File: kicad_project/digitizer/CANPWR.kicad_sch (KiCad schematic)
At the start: 4 parts

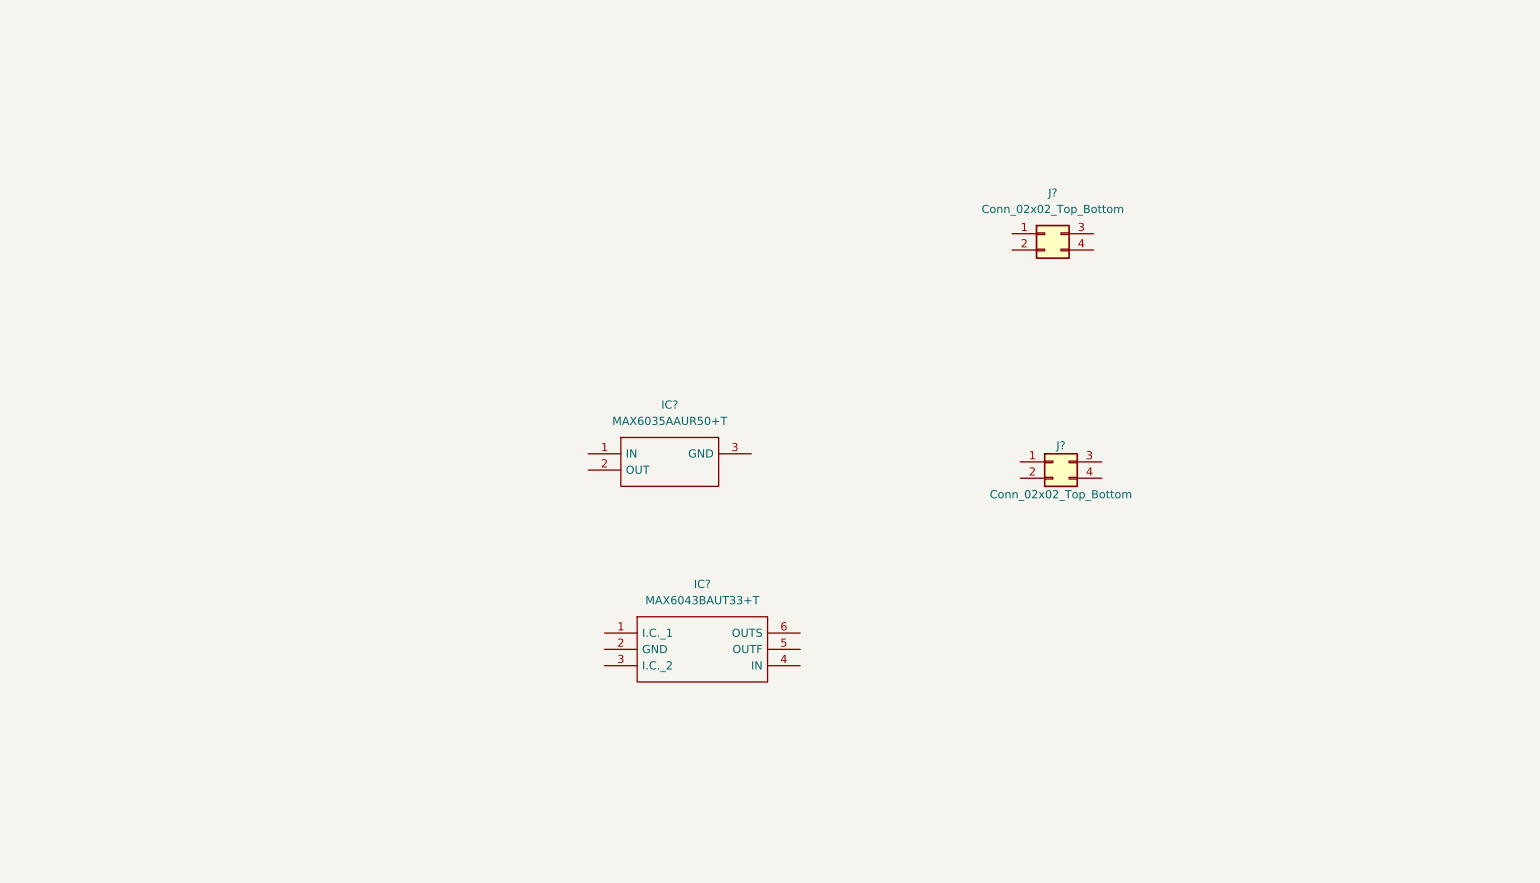
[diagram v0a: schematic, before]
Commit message: finished the CANPWR sheet, got to work on the MCU sheet (finished the CAN stuff). Good progress; still missing the MCU pin connections and the connector footprints (M12, deutsch, etc.)
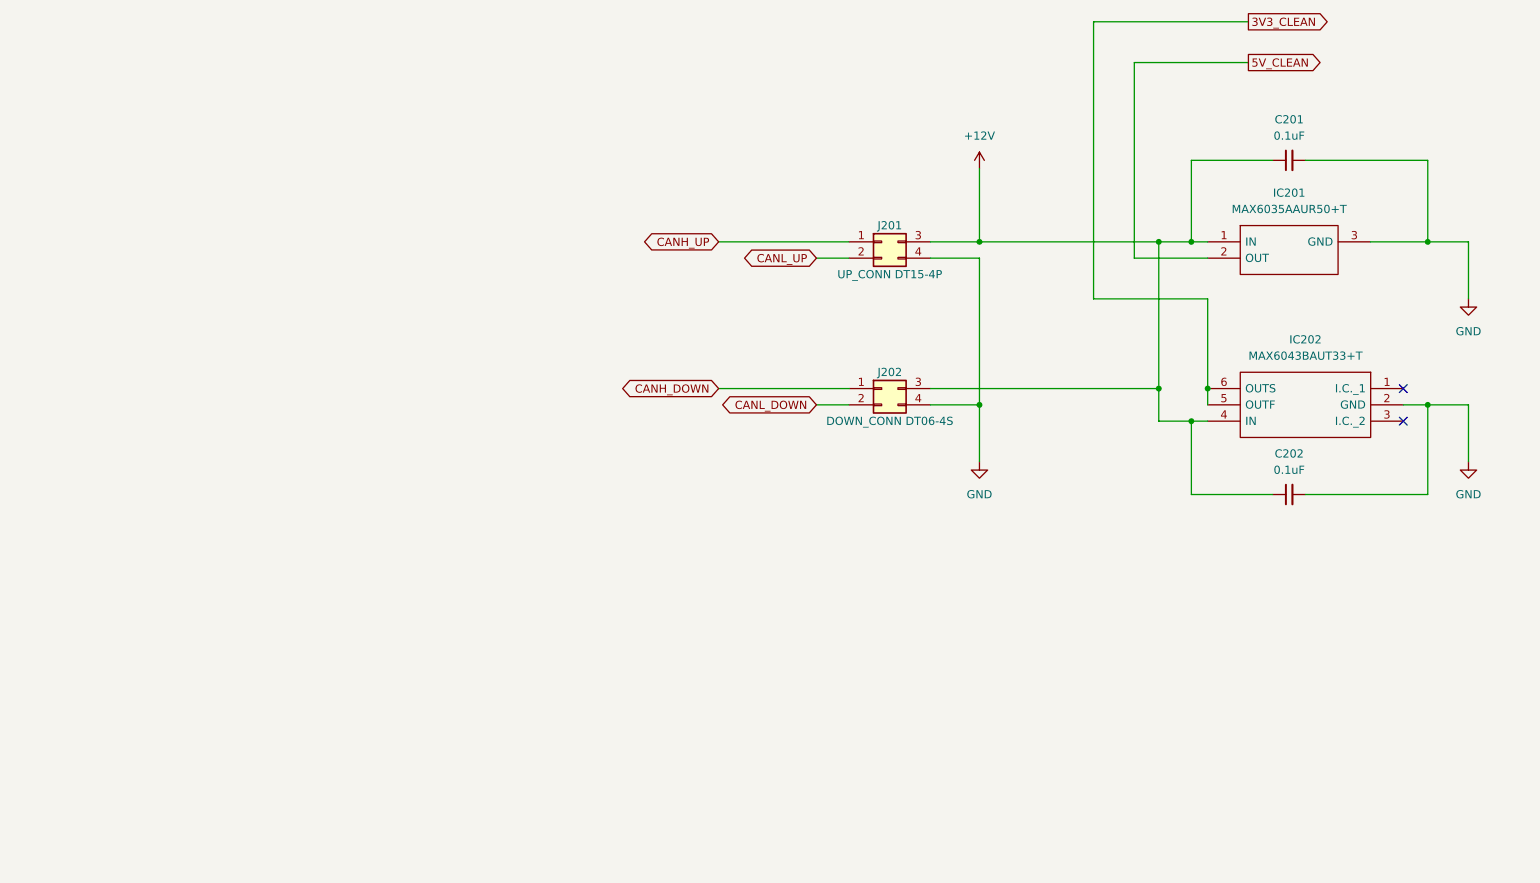
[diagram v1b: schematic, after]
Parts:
- added C201, C202: 0.1uF, Capacitor_SMD:C_2220_5650Metric_Pad1.97x5.40mm_HandSolder, symbol Device:C_Small
- J201: renamed from J?; value Conn_02x02_Top_Bottom -> UP_CONN DT15-4P
- J202: renamed from J?; value Conn_02x02_Top_Bottom -> DOWN_CONN DT06-4S
- gave numbers to parts that had none: 2
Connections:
- net +12V: now reaches IC201.1 (IN)
- net +12V: now also IC202.4 (IN), J201.3 (Pin_3), J202.3 (Pin_3), C201.1, C202.1
- net 5V_CLEAN: now reaches IC201.2 (OUT)
- net GND: now reaches IC201.3 (GND)
- net GND: now also IC202.2 (GND), J201.4 (Pin_4), J202.4 (Pin_4), C201.2, C202.2
- net 3V3_CLEAN: now reaches IC202.5 (OUTF)
- net 3V3_CLEAN: now also IC202.6 (OUTS)
- net CANH_UP: now reaches J201.1 (Pin_1)
- net CANL_UP: now reaches J201.2 (Pin_2)
- net CANH_DOWN: now reaches J202.1 (Pin_1)
- net CANL_DOWN: now reaches J202.2 (Pin_2)
- no-connect marks 0 -> 2
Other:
- moved on the sheet: IC201, IC202, J201, J202

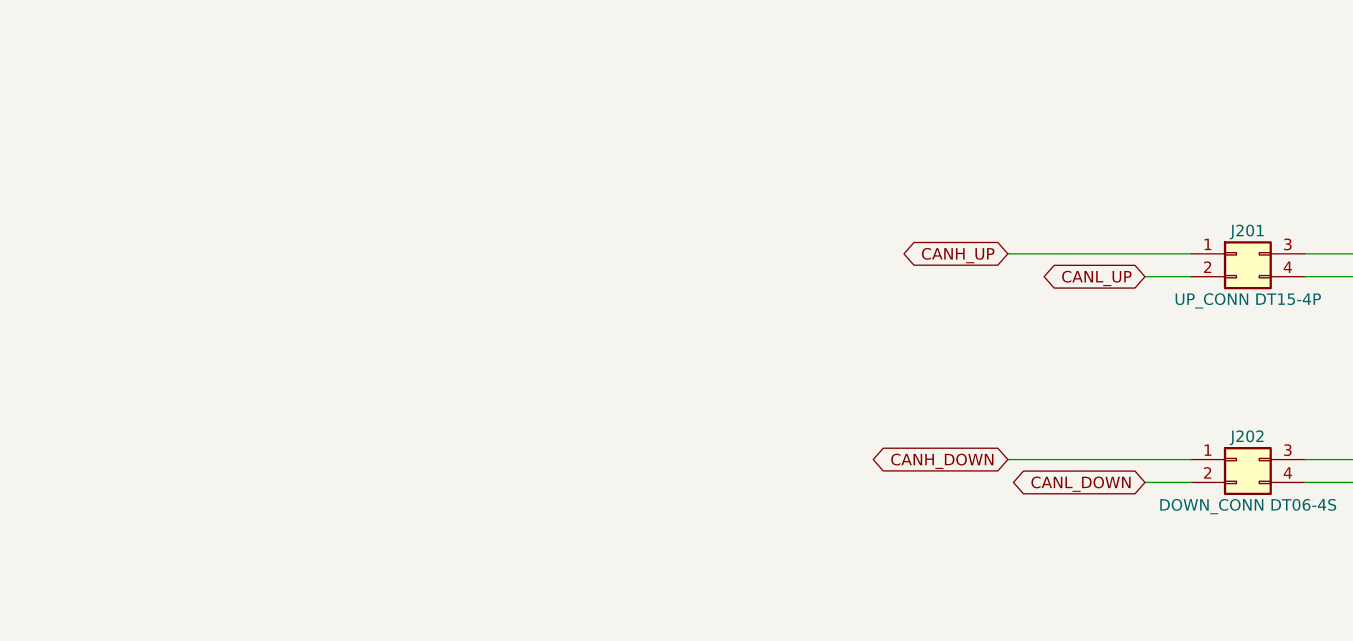
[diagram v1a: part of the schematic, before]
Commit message: moved CAN modules to the CANPWR sheet. Finished (first draft) of the MCU power design
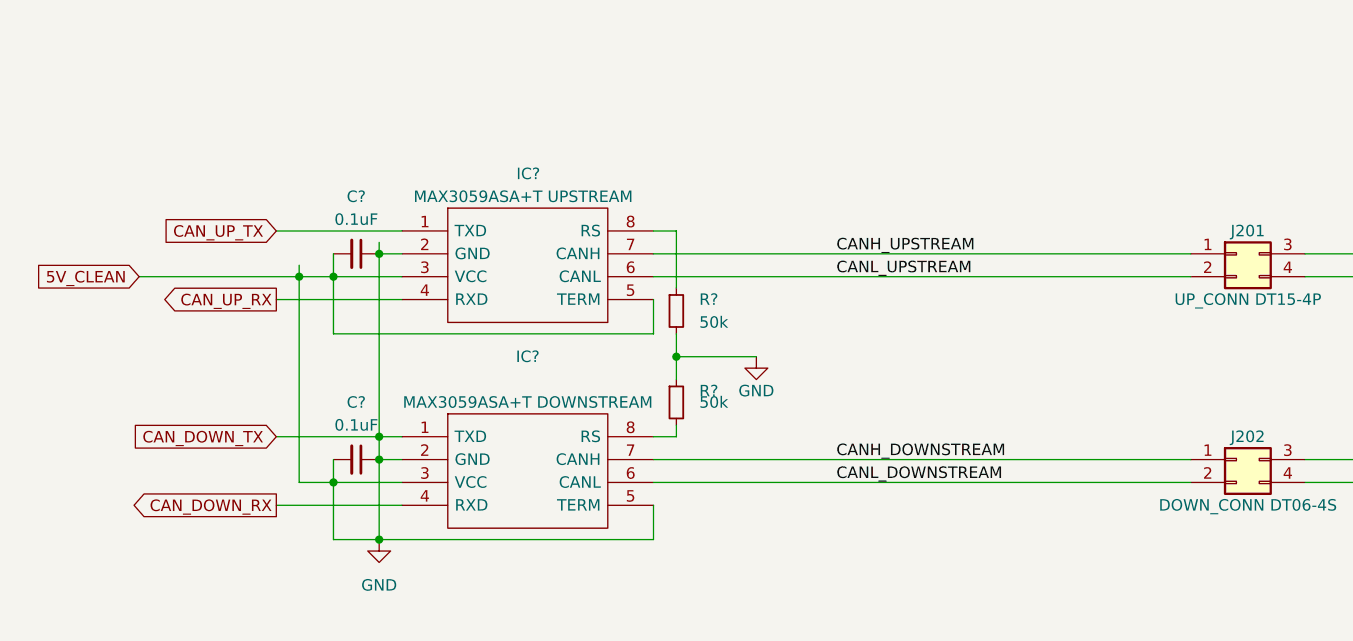
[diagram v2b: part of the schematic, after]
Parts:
- added C? (x2): 0.1uF, Capacitor_SMD:C_2220_5650Metric_Pad1.97x5.40mm_HandSolder, symbol Device:C_Small
- added IC?: MAX3059ASA+T DOWNSTREAM, SOIC127P600X175-8N, symbol SamacSys_Parts:MAX3059ASA+T
- added IC?: MAX3059ASA+T UPSTREAM, SOIC127P600X175-8N, symbol SamacSys_Parts:MAX3059ASA+T
- added R? (x2): 50k, Resistor_SMD:R_2512_6332Metric_Pad1.40x3.35mm_HandSolder, symbol Device:R_Small
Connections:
- net 5V_CLEAN is gone; now on net GND: IC201.2 (OUT)
- net GND: now also C?.1, C?.1, C?.2, C?.2, IC?.1 (TXD), IC?.2 (GND), IC?.2 (GND), IC?.3 (VCC), IC?.3 (VCC), IC?.5 (TERM), IC?.5 (TERM), R?.1, R?.2
- net CANH_DOWN renamed CANH_DOWNSTREAM
- net CANH_DOWNSTREAM: now also IC?.7 (CANH)
- net CANH_UP renamed CANH_UPSTREAM
- net CANH_UPSTREAM: now also IC?.7 (CANH)
- net CANL_DOWN renamed CANL_DOWNSTREAM
- net CANL_DOWNSTREAM: now also IC?.6 (CANL)
- net CANL_UP renamed CANL_UPSTREAM
- net CANL_UPSTREAM: now also IC?.6 (CANL)
- new net: IC?.8 (RS), R?.2
- new net: IC?.8 (RS), R?.1
- new net CAN_DOWN_RX: IC?.4 (RXD)
- new net CAN_UP_RX: IC?.4 (RXD)
- new net CAN_UP_TX: IC?.1 (TXD)

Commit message: updated annotations
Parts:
- gave numbers to parts that had none: 6
- renumbered C201 to C203, C202 to C204, IC201 to IC203, IC202 to IC204
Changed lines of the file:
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@@
   (symbol (lib_id "Device:C_Small") (at 62.23 60.96 270) (unit 1)
     (in_bom yes) (on_board yes)
-    (property "Reference" "C?" (id 0) (at 62.23 54.61 90))
+    (property "Reference" "C201" (id 0) (at 62.23 54.61 90))
     (property "Value" "0.1uF" (id 1) (at 62.23 57.15 90))
     (property "Footprint" "Capacitor_SMD:C_2220_5650Metric_Pad1.97x5.40mm_HandSolder" (id 2) (at 62.23 60.96 0)
@@
   (symbol (lib_id "Device:R_Small") (at 97.79 77.47 0) (unit 1)
     (in_bom yes) (on_board yes)
-    (property "Reference" "R?" (id 0) (at 100.33 76.1999 0)
+    (property "Reference" "R202" (id 0) (at 100.33 76.1999 0)
       (effects (font (size 1.27 1.27)) (justify left))
     )
@@
   (symbol (lib_id "SamacSys_Parts:MAX3059ASA+T") (at 67.31 81.28 0) (unit 1)
     (in_bom yes) (on_board yes)
-    (property "Reference" "IC?" (id 0) (at 81.28 72.39 0))
+    (property "Reference" "IC202" (id 0) (at 81.28 72.39 0))
     (property "Value" "MAX3059ASA+T DOWNSTREAM" (id 1) (at 81.28 77.47 0))
     (property "Footprint" "SOIC127P600X175-8N" (id 2) (at 91.44 78.74 0)
@@
   (symbol (lib_id "Device:R_Small") (at 97.79 67.31 0) (unit 1)
     (in_bom yes) (on_board yes) (fields_autoplaced)
-    (property "Reference" "R?" (id 0) (at 100.33 66.0399 0)
+    (property "Reference" "R201" (id 0) (at 100.33 66.0399 0)
       (effects (font (size 1.27 1.27)) (justify left))
     )
@@
   (symbol (lib_id "SamacSys_Parts:MAX6035AAUR50+T") (at 210.82 60.96 0) (unit 1)
     (in_bom yes) (on_board yes) (fields_autoplaced)
-    (property "Reference" "IC201" (id 0) (at 223.52 53.34 0))
+    (property "Reference" "IC203" (id 0) (at 223.52 53.34 0))
     (property "Value" "MAX6035AAUR50+T" (id 1) (at 223.52 55.88 0))
     (property "Footprint" "SOT95P237X112-3N" (id 2) (at 232.41 58.42 0)
@@
   (symbol (lib_id "power:GND") (at 251.46 69.85 0) (unit 1)
     (in_bom yes) (on_board yes) (fields_autoplaced)
-    (property "Reference" "#PWR0203" (id 0) (at 251.46 76.2 0)
+    (property "Reference" "#PWR0205" (id 0) (at 251.46 76.2 0)
       (effects (font (size 1.27 1.27)) hide)
     )
@@
   (symbol (lib_id "power:+12V") (at 175.26 49.53 0) (unit 1)
     (in_bom yes) (on_board yes) (fields_autoplaced)
-    (property "Reference" "#PWR0201" (id 0) (at 175.26 53.34 0)
+    (property "Reference" "#PWR0203" (id 0) (at 175.26 53.34 0)
       (effects (font (size 1.27 1.27)) hide)
     )
@@
   (symbol (lib_id "power:GND") (at 251.46 95.25 0) (unit 1)
     (in_bom yes) (on_board yes) (fields_autoplaced)
-    (property "Reference" "#PWR0204" (id 0) (at 251.46 101.6 0)
+    (property "Reference" "#PWR0206" (id 0) (at 251.46 101.6 0)
       (effects (font (size 1.27 1.27)) hide)
     )
@@
   (symbol (lib_id "SamacSys_Parts:MAX6043BAUT33+T") (at 241.3 83.82 0) (mirror y) (unit 1)
     (in_bom yes) (on_board yes) (fields_autoplaced)
-    (property "Reference" "IC202" (id 0) (at 226.06 76.2 0))
+    (property "Reference" "IC204" (id 0) (at 226.06 76.2 0))
     (property "Value" "MAX6043BAUT33+T" (id 1) (at 226.06 78.74 0))
     (property "Footprint" "SOT95P280X145-6N" (id 2) (at 214.63 81.28 0)
@@
   (symbol (lib_id "power:GND") (at 175.26 95.25 0) (unit 1)
     (in_bom yes) (on_board yes) (fields_autoplaced)
-    (property "Reference" "#PWR0202" (id 0) (at 175.26 101.6 0)
+    (property "Reference" "#PWR0204" (id 0) (at 175.26 101.6 0)
       (effects (font (size 1.27 1.27)) hide)
     )
@@
   (symbol (lib_id "Device:C_Small") (at 223.52 48.26 90) (unit 1)
     (in_bom yes) (on_board yes) (fields_autoplaced)
-    (property "Reference" "C201" (id 0) (at 223.5263 41.91 90))
+    (property "Reference" "C203" (id 0) (at 223.5263 41.91 90))
     (property "Value" "0.1uF" (id 1) (at 223.5263 44.45 90))
     (property "Footprint" "Capacitor_SMD:C_2220_5650Metric_Pad1.97x5.40mm_HandSolder" (id 2) (at 223.52 48.26 0)
@@
   (symbol (lib_id "SamacSys_Parts:MAX3059ASA+T") (at 67.31 58.42 0) (unit 1)
     (in_bom yes) (on_board yes)
-    (property "Reference" "IC?" (id 0) (at 80.01 52.07 0)
+    (property "Reference" "IC201" (id 0) (at 80.01 52.07 0)
       (effects (font (size 1.27 1.27)) (justify left))
     )
@@
   (symbol (lib_id "power:GND") (at 64.77 92.71 0) (unit 1)
     (in_bom yes) (on_board yes) (fields_autoplaced)
-    (property "Reference" "#PWR?" (id 0) (at 64.77 99.06 0)
+    (property "Reference" "#PWR0201" (id 0) (at 64.77 99.06 0)
       (effects (font (size 1.27 1.27)) hide)
     )
@@
   (symbol (lib_id "power:GND") (at 106.68 72.39 0) (unit 1)
     (in_bom yes) (on_board yes)
-    (property "Reference" "#PWR?" (id 0) (at 106.68 78.74 0)
+    (property "Reference" "#PWR0202" (id 0) (at 106.68 78.74 0)
       (effects (font (size 1.27 1.27)) hide)
     )
@@
   (symbol (lib_id "Device:C_Small") (at 62.23 83.82 270) (unit 1)
     (in_bom yes) (on_board yes)
-    (property "Reference" "C?" (id 0) (at 62.23 77.47 90))
+    (property "Reference" "C202" (id 0) (at 62.23 77.47 90))
     (property "Value" "0.1uF" (id 1) (at 62.23 80.01 90))
     (property "Footprint" "Capacitor_SMD:C_2220_5650Metric_Pad1.97x5.40mm_HandSolder" (id 2) (at 62.23 83.82 0)
@@
   (symbol (lib_id "Device:C_Small") (at 223.52 100.33 90) (unit 1)
     (in_bom yes) (on_board yes) (fields_autoplaced)
-    (property "Reference" "C202" (id 0) (at 223.5263 93.98 90))
+    (property "Reference" "C204" (id 0) (at 223.5263 93.98 90))
     (property "Value" "0.1uF" (id 1) (at 223.5263 96.52 90))
     (property "Footprint" "Capacitor_SMD:C_2220_5650Metric_Pad1.97x5.40mm_HandSolder" (id 2) (at 223.52 100.33 0)
